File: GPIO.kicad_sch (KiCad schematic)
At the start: 35 parts, among them J11 74LS245, J9 uPD446, K15 74LS04, U1 74LS245, U2 74LS10

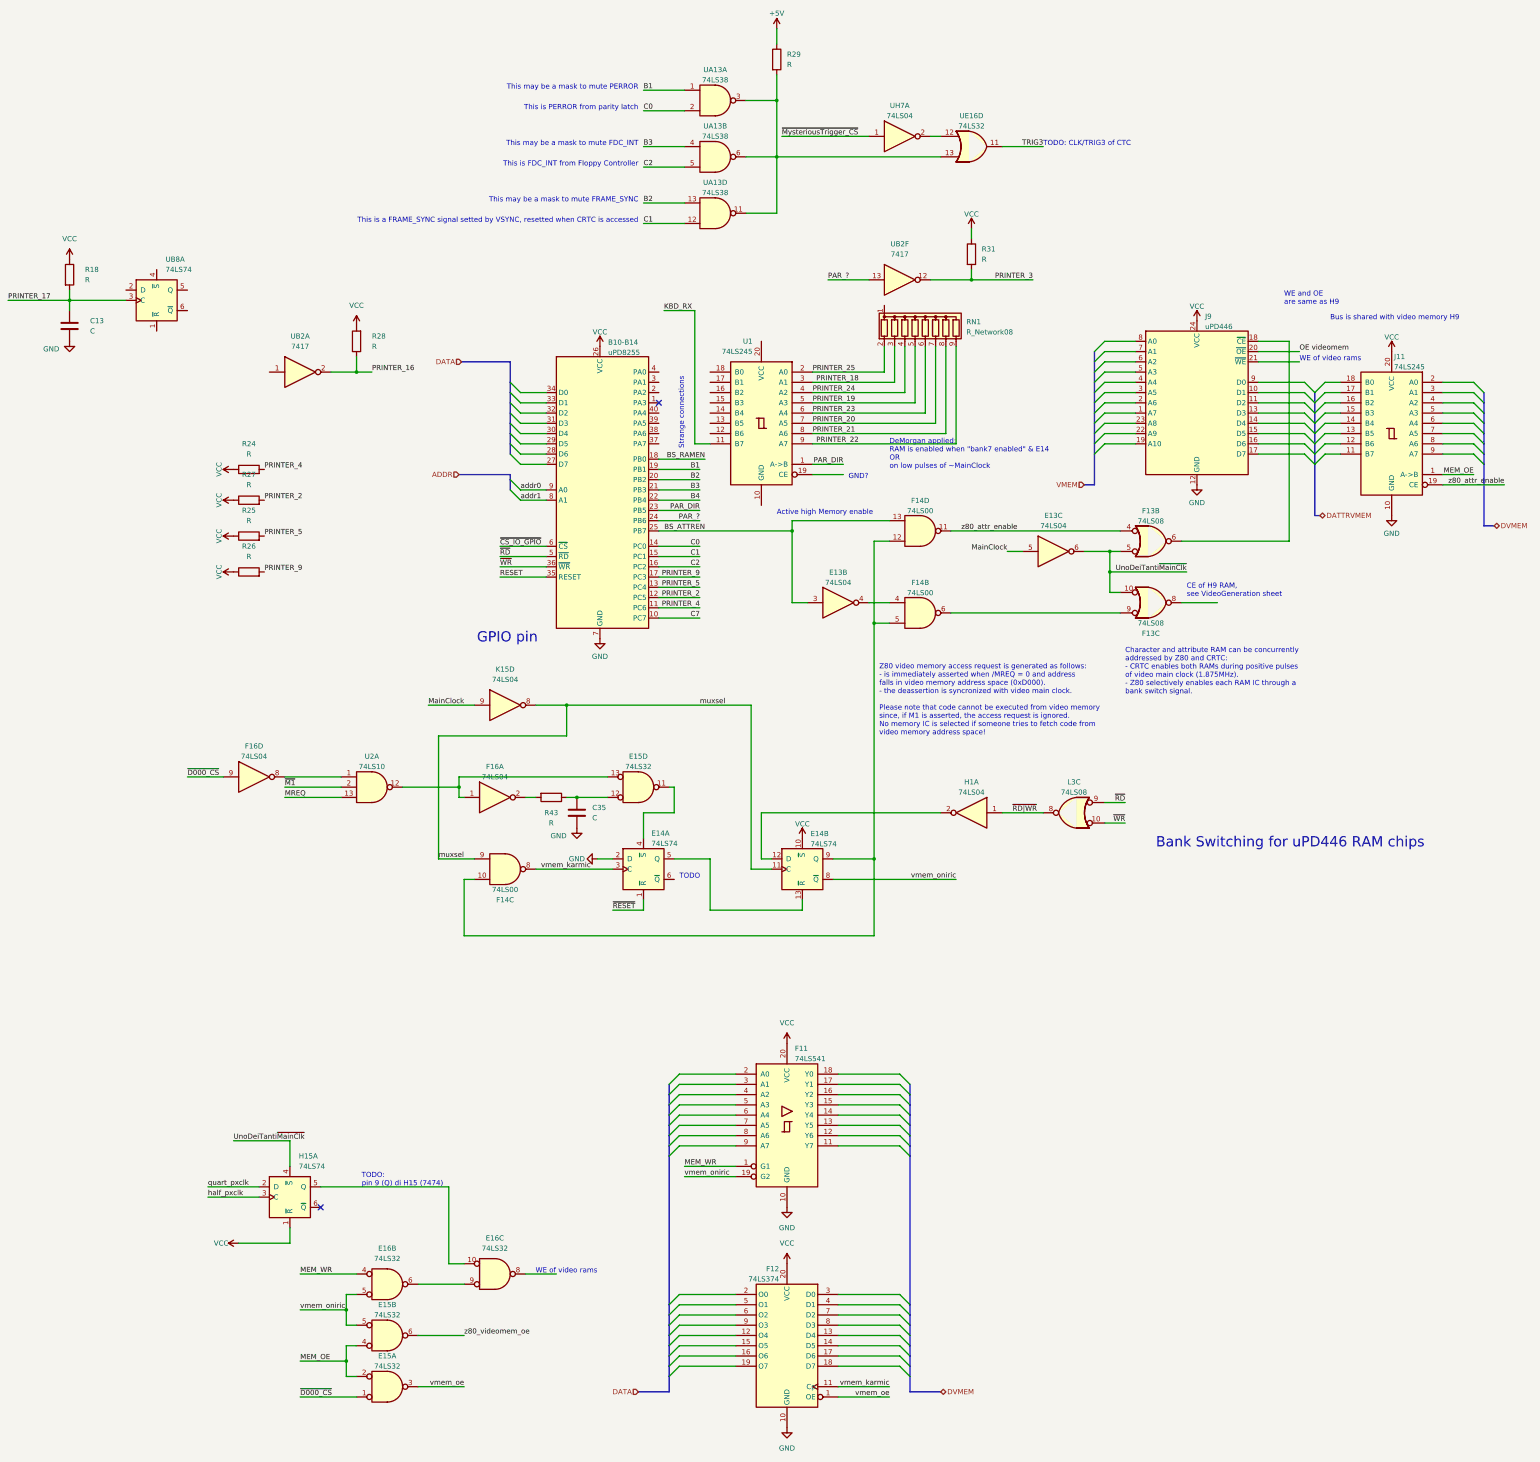
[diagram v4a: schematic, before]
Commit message: Schematics refactoring:
- New sheet reserved to video memory.
- Removed video memory parts inside video_generation.
- Removed video memory parts inside GPIO.
- Generic cleanup to keep all circuits inside each sheet.
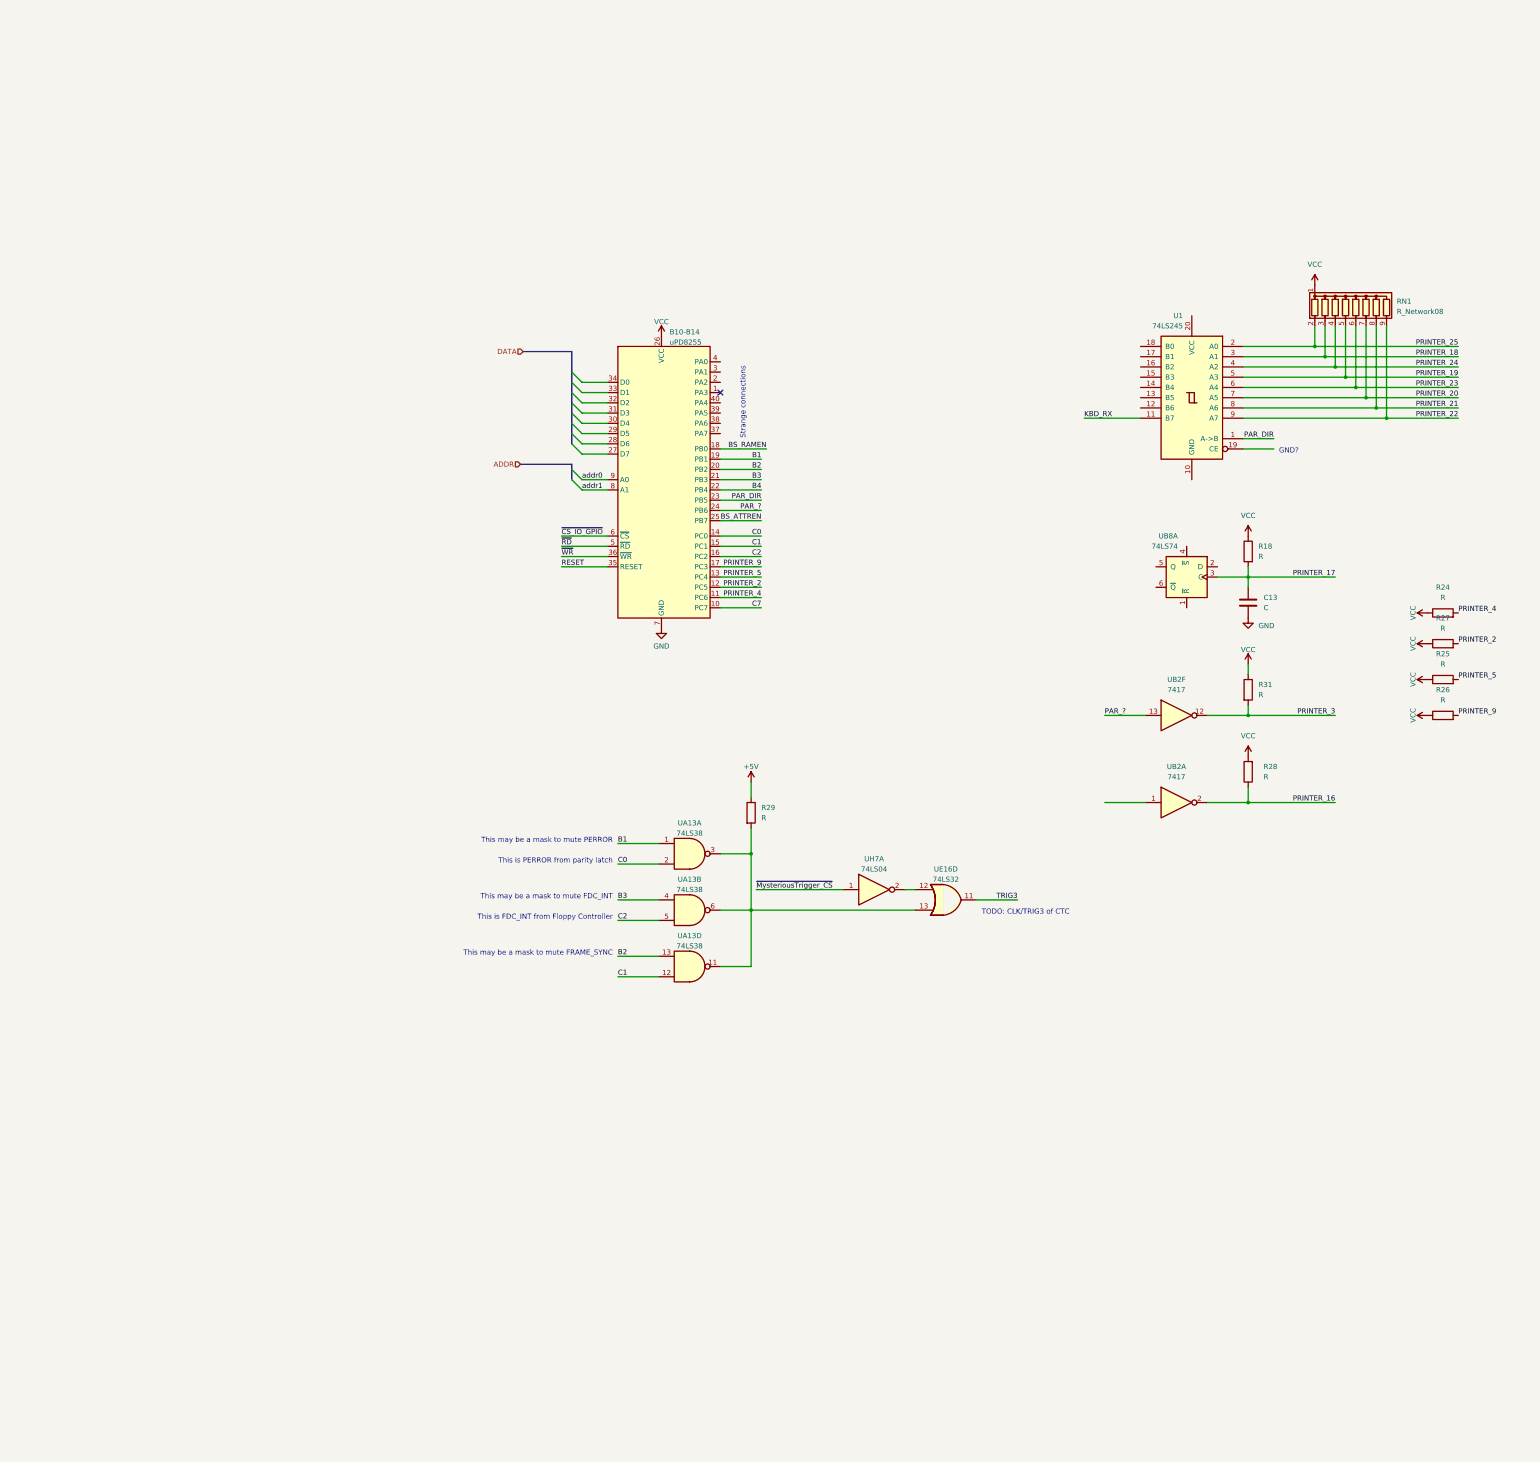
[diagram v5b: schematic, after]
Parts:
- removed C35: C, symbol Device:C
- removed E13, F16, H1, K15: 74LS04, symbol 74xx:74LS04
- removed E14, H15: 74LS74, symbol 74xx:74LS74
- removed E15, E16: 74LS32, symbol 74xx:74LS32
- removed F11: 74LS541, symbol 74xx:74LS541
- removed F12: 74LS374, symbol 74xx:74LS374
- removed F13, L3: 74LS08, symbol 74xx:74LS08
- removed F14: 74LS00, symbol 74xx:74LS00
- removed J11: 74LS245, symbol 74xx:74LS245
- removed J9: uPD446, symbol ceda:uPD446
- removed R43: R, symbol Device:R
- removed U2: 74LS10, symbol 74xx:74LS10
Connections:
- net VCC: now also RN1.1 (common)
- no-connect marks 2 -> 1
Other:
- note removed: "Active high Memory enable"
- note removed: "Bank Switching for uPD446 RAM chips"
- note removed: "Bus is shared with video memory H9"
- note removed: "CE of H9 RAM, see VideoGeneration sheet"
- note removed: "Character and attribute RAM can be concurrently addressed by Z80 and CRTC: - CRTC enables both RAMs during positive pulses of video main clock (1.875MHz). - Z80 selectively enables each RAM IC through a bank switch signal."
- note removed: "DeMorgan applied: RAM is enabled when "bank7 enabled" & E14 OR on low pulses of ~MainClock"
- note removed: "GPIO pin"
- note removed: "TODO"
- note removed: "TODO: pin 9 (Q) di H15 (7474)"
- note removed: "This is a FRAME_SYNC signal setted by VSYNC, resetted when CRTC is accessed"
- note removed: "WE and OE are same as H9"
- note removed: "WE of video rams"
- note removed: "Z80 video memory access request is generated as follows: - is immediately asserted when /MREQ = 0 and address falls in video memory address space (0xD000). - the deassertion is syncronized with video main clock. Please note that code cannot be executed from video memory since, if M1 is asserted, the access request is ignored. No memory IC is selected if someone tries to fetch code from video memo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"
- moved on the sheet: B10-B14, C13, R18, R24, R25, R26, R27, R28, R29, R31, RN1, U1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

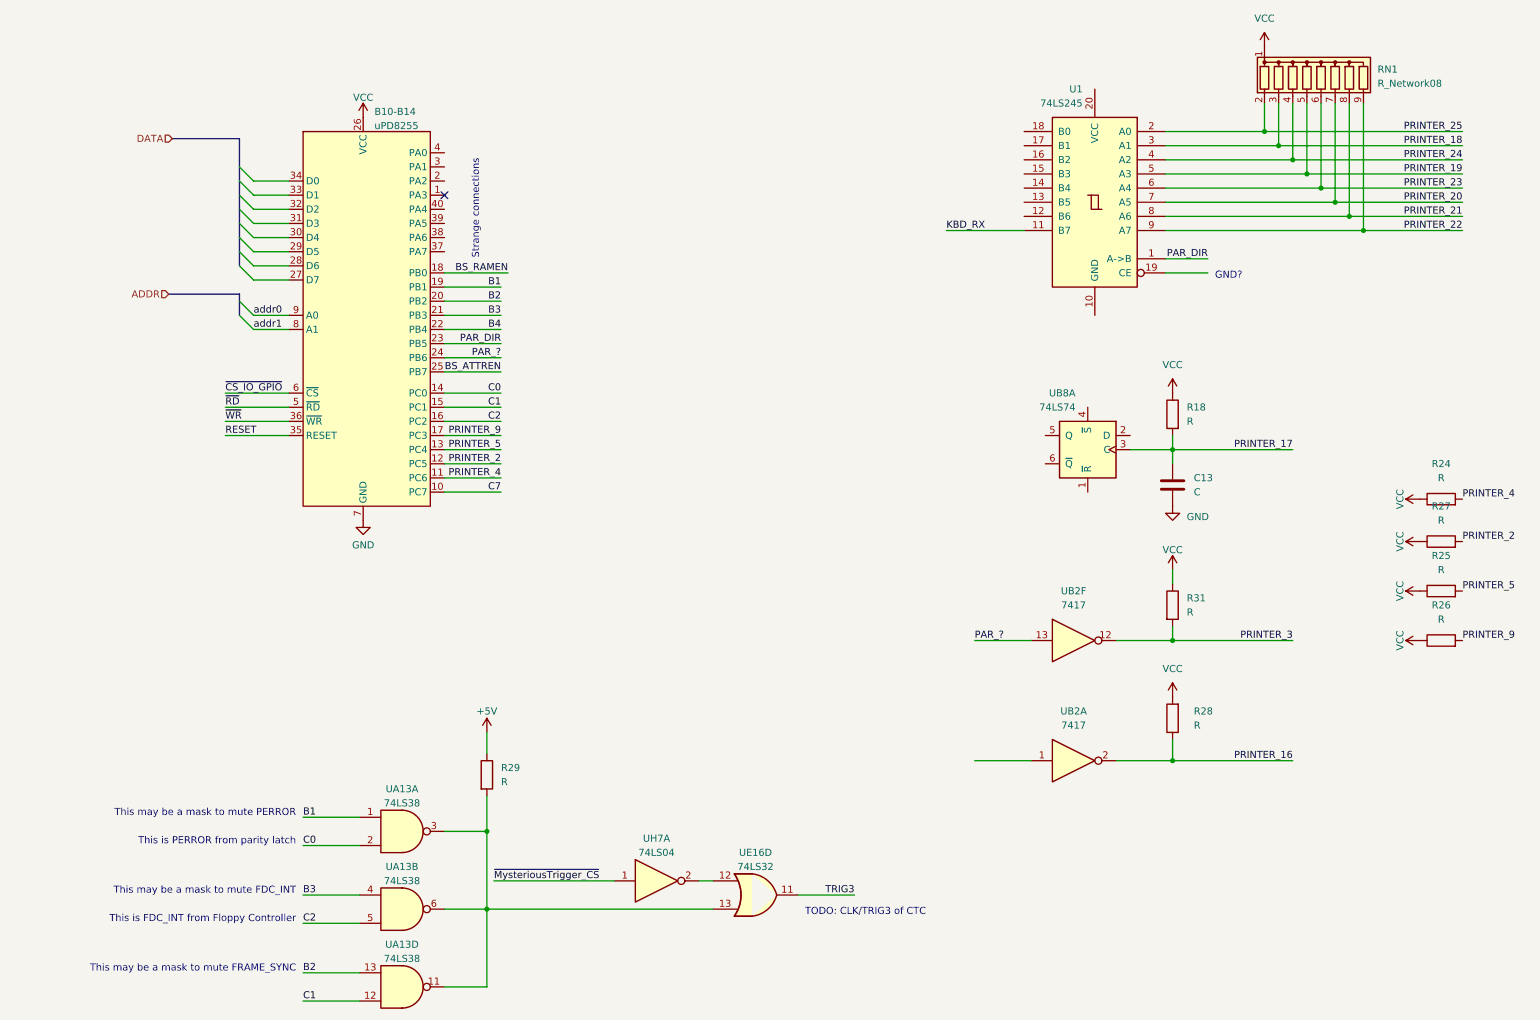
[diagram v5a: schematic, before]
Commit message: GPIO: wire renaming
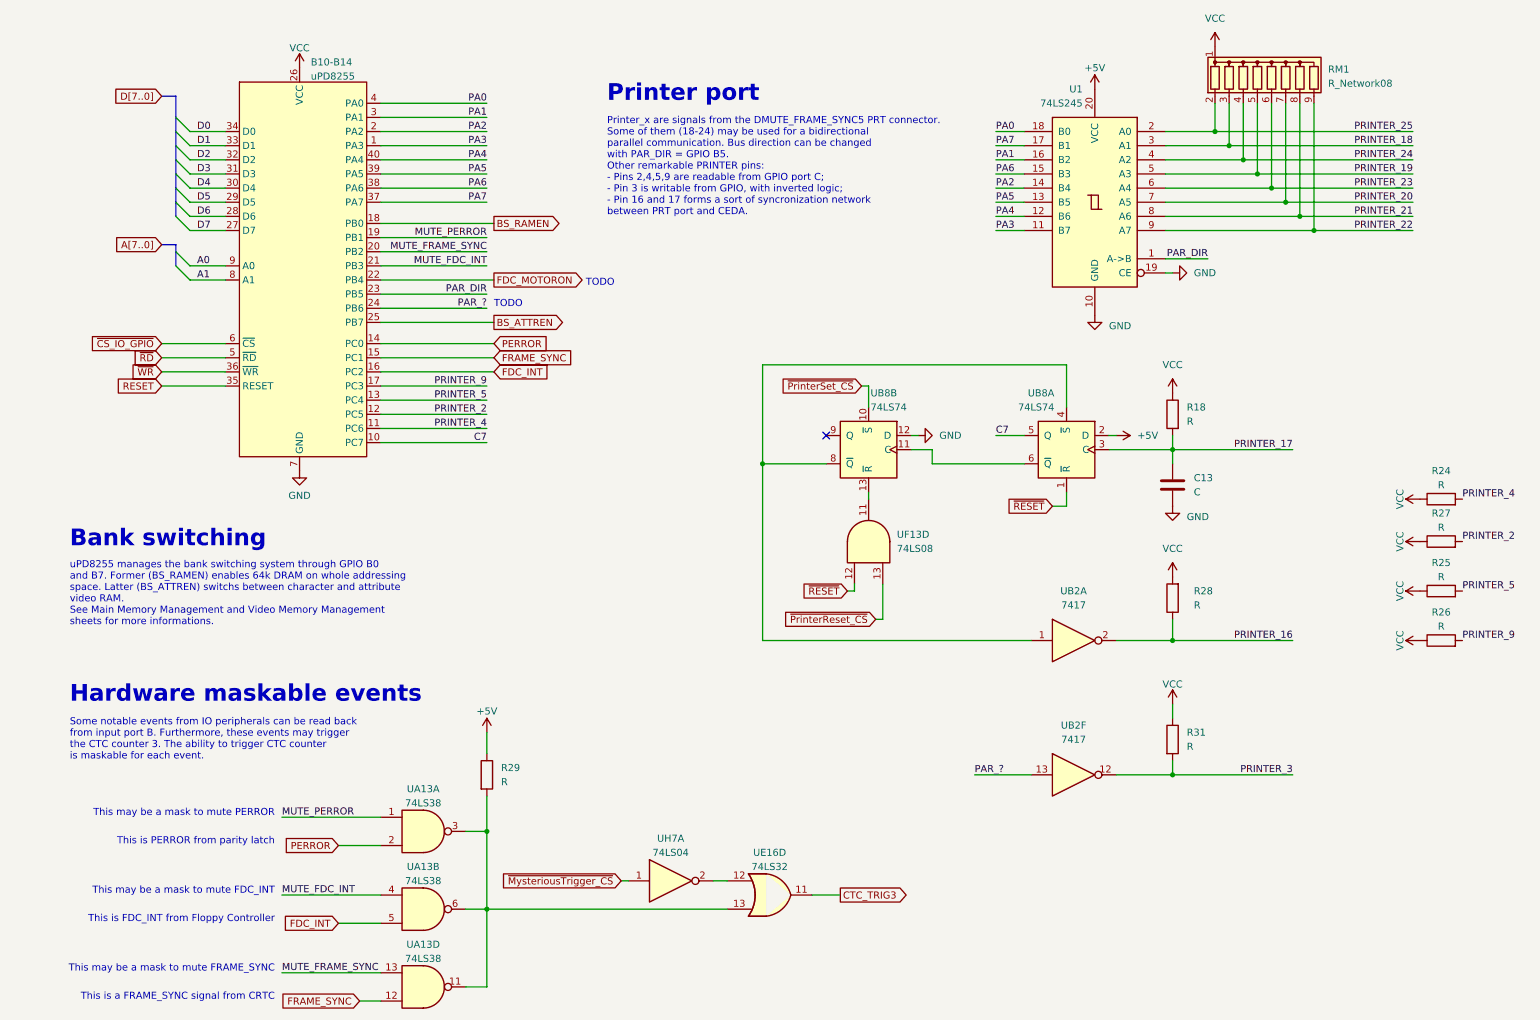
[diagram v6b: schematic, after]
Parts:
- added unit 2 of UB8
- added UF13: 74LS08, symbol 74xx:74LS08
- renumbered RN1 to RM1
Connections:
- net KBD_RX is gone; now on net PA3: U1.11 (B7)
- net +5V: now also U1.20 (VCC), UB8.2 (D)
- net C7: now also UB8.5 (Q)
- net GND: now also U1.10 (GND), U1.19 (CE), UB8.12 (D)
- net ~{RESET}: now reaches UB8.1 (~{R})
- net ~{RESET}: now also UF13.12
- net at UB8.4 (~{S}): now also UB2.1, UB8.8 (~{Q})
- net at UB8.6 (~{Q}): now also UB8.11 (C)
- net PA3: now reaches B10-B14.1 (PA3)
- net PA2: now reaches B10-B14.2 (PA2)
- net PA2: now also U1.14 (B4)
- net D7: now reaches B10-B14.27 (D7)
- net D6: now reaches B10-B14.28 (D6)
- net D5: now reaches B10-B14.29 (D5)
- net PA1: now reaches B10-B14.3 (PA1)
- net PA1: now also U1.16 (B2)
- net D4: now reaches B10-B14.30 (D4)
- net D3: now reaches B10-B14.31 (D3)
- net D2: now reaches B10-B14.32 (D2)
- net D1: now reaches B10-B14.33 (D1)
- net D0: now reaches B10-B14.34 (D0)
- net PA7: now reaches B10-B14.37 (PA7)
- net PA7: now also U1.17 (B1)
- net PA6: now reaches B10-B14.38 (PA6)
- net PA6: now also U1.15 (B3)
- net PA5: now reaches B10-B14.39 (PA5)
- net PA5: now also U1.13 (B5)
- net PA0: now reaches B10-B14.4 (PA0)
- net PA0: now also U1.18 (B0)
- net PA4: now reaches B10-B14.40 (PA4)
- net PA4: now also U1.12 (B6)
- net B1 renamed MUTE_PERROR
- net B2 renamed MUTE_FRAME_SYNC
- net B3 renamed MUTE_FDC_INT
- net B4 renamed FDC_MOTORON
- net C0 renamed PERROR
- net C1 renamed FRAME_SYNC
- net C2 renamed FDC_INT
- net TRIG3 renamed CTC_TRIG3
- net addr0 renamed A0
- net addr1 renamed A1
- new net: UB8.13 (~{R}), UF13.11
- new net ~{PrinterReset_CS}: UF13.13
- new net ~{PrinterSet_CS}: UB8.10 (~{S})
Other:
- note added: "Bank switching"
- note added: "Hardware maskable events"
- note added: "Printer port"
- note added: "Printer_x are signals from the DMUTE_FRAME_SYNC5 PRT connector. Some of them (18-24) may be used for a bidirectional parallel communication. Bus direction can be changed with PAR_DIR = GPIO B5. Other remarkable PRINTER pins: - Pins 2,4,5,9 are readable from GPIO port C; - Pin 3 is writable from GPIO, with inverted logic; - Pin 16 and 17 forms a sort of syncronization network between PRT port and 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"
- note added: "Some notable events from IO peripherals can be read back from input port B. Furthermore, these events may trigger the CTC counter 3. The ability to trigger CTC counter is maskable for each event."
- note added: "TODO"
- note added: "This is a FRAME_SYNC signal from CRTC"
- note added: "uPD8255 manages the bank switching system through GPIO B0 and B7. Former (BS_RAMEN) enables 64k DRAM on whole addressing space. Latter (BS_ATTREN) switchs between character and attribute video RAM. See Main Memory Management and Video Memory Management sheets for more informations."
- note removed: "GND?"
- note removed: "Strange connections"
- note removed: "TODO: CLK/TRIG3 of CTC"
- moved on the sheet: B10-B14, R28, R31, RM1, UA13A, UA13B, UA13D, UB2A, UB2F, UB8A, UE16D, UH7A
